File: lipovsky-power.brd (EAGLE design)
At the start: 59 x 32 mm, 95 parts, among them J1 M04-929J, J2 M04-929J, J3 M04-929J, J4 M04-929J, Q1 NMOS30V_30A, Q12 NMOS40V_10A, Q14 NMOS40V_10A, Q16 NMOS40V_10A, Q18 NMOS40V_10A, Q21 PMOS30V_11A, Q22 PMOS30V_11A, Q23 NMOS40V_10A, Q24 NMOS40V_10A, Q25 PMOS30V_11A, Q26 PMOS30V_11A, Q27 NMOS40V_10A, Q28 NMOS40V_10A, Q3 2PMOS50V_0.17A, Q31 PMOS30V_11A, Q32 PMOS30V_11A, Q33 PMOS30V_11A, Q34 PMOS30V_11A, Q35 PMOS30V_11A, Q36 PMOS30V_11A, Q37 PMOS30V_11A, Q38 PMOS30V_11A, Q4 2PMOS50V_0.17A, Q41 PMOS30V_11A, Q42 PMOS30V_11A, Q43 PMOS30V_11A, Q44 PMOS30V_11A, Q45 PMOS30V_11A, Q46 PMOS30V_11A, Q47 PMOS30V_11A, Q48 PMOS30V_11A, Q5 2NMOS30V_0.1A, Q51 PMOS30V_11A, Q52 PMOS30V_11A, Q53 PMOS30V_11A, Q54 PMOS30V_11A, Q55 PMOS30V_11A, Q56 PMOS30V_11A, Q57 PMOS30V_11A, Q58 PMOS30V_11A, Q62 PMOS30V_11A, Q64 PMOS30V_11A, Q66 PMOS30V_11A, Q68 PMOS30V_11A, T1 TFORM_4_4311_4A4, U1 DG508BEN-T1-GE4, U2 DG508BEN-T1-GE4, U4 LTC3805-5IDD, U6 AR30N60PPA-13

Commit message: tidy
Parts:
- MVOE: value ATTINYX4A4MMH -> ATTINYX4A2MMHR
- moved R16 2.39 mm to (43.0, 26.1), turned to 90 degrees
- moved C8 1.64 mm to (41.9, 26.8)
- moved RGS 0.22 mm to (19.2, 25.1)
- moved R10 0.20 mm to (43.4, 28.0)
- moved RGS6 0.10 mm to (26.5, 25.8)
- turned R3 to 0 degrees
- turned R4 to 0 degrees
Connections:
- removed net !RESET: J3.4, MVOE.13, R3.2
- new net !S_RESET: J3.4, MVOE.13, R3.1
- net +5V: now also R3.2, R4.2; no longer R3.1, R4.1
- net SDA: now also R4.1; no longer R4.2
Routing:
- net !RESET: track 9.34 -> 0.00 mm, vias 1 -> 0
- net !S_RESET: track 0.00 -> 9.34 mm, vias 0 -> 1
- net S-: track 142.4 -> 138.3 mm, vias 19 -> 18
- net EN_FLYBACK: track 11.8 -> 10.1 mm, vias 3 -> 2
- net +5V: track 41.9 -> 41.3 mm
- net AS2: track 23.2 -> 22.7 mm, vias 3 -> 2
- net AS1: track 23.7 -> 23.4 mm, vias 3 -> 2
- net AS0: track 24.2 -> 24.1 mm, vias 3 -> 2
- net BATT-: vias 40 -> 41

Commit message: Moved fet
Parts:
- moved Q3 19.4 mm to (15.4, 7.60), turned to 180 degrees
- moved C7 4.00 mm to (16.4, 26.7)
- moved RGS-2 3.86 mm to (13.0, 6.40)
- moved RGS1 2.50 mm to (16.8, 6.40)
- moved C1 2.02 mm to (14.0, 6.40)
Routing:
- net !GS1: track 7.31 -> 34.9 mm
- net GS1: track 28.9 -> 11.7 mm, vias 4 -> 2
- net GS-2: track 33.1 -> 16.5 mm, vias 4 -> 3
- net GS+2: track 30.9 -> 37.7 mm, vias 4 -> 5
- net C4+: track 52.4 -> 46.9 mm, vias 4 -> 3
- net BATT+: track 69.9 -> 69.2 mm
- net BATT-: vias 41 -> 42

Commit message: tidy
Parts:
- moved TP1 1.00 mm to (41.0, 30.0)
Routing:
- net S-: track 138.3 -> 142.7 mm, vias 18 -> 19
- net MISO: track 4.87 -> 5.87 mm
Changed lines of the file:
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@@
 <vertex x="28" y="11.175"/>
 </polygon>
-<text x="41.1" y="30" size="0.8" layer="22" font="vector" ratio="15" distance="75" rot="MR90" align="top-center">MISO</text>
+<text x="40.1" y="30.1" size="0.8" layer="22" font="vector" ratio="15" distance="75" rot="MR90" align="top-center">MISO</text>
 </plain>
 <attributes>
@@
 <attribute name="TEMP" value="±100ppm/°C" x="43" y="26.1" size="1.778" layer="27" rot="R90" display="off"/>
 </element>
-<element name="TP1" library="SparkFun-Passives" package="PAD.03X.03" value="TEST-POINT3" x="42" y="30" rot="MR0"/>
+<element name="TP1" library="SparkFun-Passives" package="PAD.03X.03" value="TEST-POINT3" x="41" y="30" rot="MR0"/>
 </elements>
 <signals>
@@
 <wire x1="32.6" y1="24.2" x2="32.6" y2="22.6" width="0.8" layer="1"/>
 <wire x1="32.6" y1="22.6" x2="32.3" y2="22.3" width="0.8" layer="1"/>
-<wire x1="27" y1="27.6" x2="30.9" y2="23.7" width="0.3" layer="15"/>
+<wire x1="27" y1="27.6" x2="30.5" y2="24.1" width="0.3" layer="15"/>
 <wire x1="25.2" y1="5.275" x2="25.2" y2="4.9" width="0.2" layer="1"/>
 <wire x1="25.2" y1="4.9" x2="25.4" y2="4.7" width="0.2" layer="1"/>
@@
 <wire x1="20.575" y1="22.95" x2="19.925" y2="22.95" width="0.7" layer="2"/>
 <wire x1="44.19" y1="6.31" x2="44.19" y2="2" width="0.3" layer="16"/>
-<wire x1="30.9" y1="23.7" x2="31.1" y2="23.3" width="0.3" layer="15"/>
 <wire x1="18" y1="23.1" x2="18.15" y2="22.95" width="0.3" layer="1"/>
 <wire x1="18.15" y1="22.95" x2="19.275" y2="22.95" width="0.3" layer="1"/>
@@
 <wire x1="49.71" y1="27.9" x2="48" y2="27.9" width="0.3" layer="16"/>
 <wire x1="48" y1="27.9" x2="47" y2="26.9" width="0.3" layer="16"/>
-<wire x1="46.5" y1="25.1" x2="46.5" y2="25.8" width="0.2" layer="1"/>
+<wire x1="46.5" y1="25.05" x2="46.5" y2="25.8" width="0.2" layer="1"/>
 <wire x1="41.7" y1="24.8" x2="42.1" y2="24.4" width="0.3" layer="16"/>
 <wire x1="42.1" y1="24.4" x2="42.1" y2="24" width="0.3" layer="16"/>
@@
 <wire x1="43" y1="25.6" x2="42.2" y2="25.6" width="0.4" layer="1"/>
 <wire x1="42.2" y1="25.6" x2="42.1" y2="25.5" width="0.4" layer="1"/>
-<wire x1="46.5" y1="25.1" x2="46.5" y2="25.05" width="0" layer="19" extent="1-1"/>
+<via x="30.5" y="23.65" extent="1-16" drill="0.4"/>
+<wire x1="31.1" y1="23.3" x2="30.5" y2="23.65" width="0.7" layer="15"/>
+<wire x1="30.5" y1="23.65" x2="30.5" y2="22.95" width="0.7" layer="15"/>
+<wire x1="30.5" y1="22.95" x2="30.5" y2="23.65" width="0.7" layer="1"/>
+<wire x1="30.5" y1="23.65" x2="31.1" y2="23.3" width="0.7" layer="1"/>
+<wire x1="30.5" y1="23.65" x2="30.5" y2="22.95" width="0.7" layer="2"/>
+<wire x1="31.1" y1="23.3" x2="30.5" y2="23.65" width="0.7" layer="2"/>
+<wire x1="31.1" y1="23.3" x2="30.5" y2="23.65" width="0.7" layer="16"/>
+<wire x1="30.5" y1="24.1" x2="30.5" y2="23.65" width="0.3" layer="15"/>
 </signal>
 <signal name="S+">
@@
 <wire x1="45.6" y1="27.85" x2="45.6" y2="28.5" width="0.2" layer="1"/>
 <contactref element="TP1" pad="P$1"/>
-<wire x1="45.6" y1="28.5" x2="43.5" y2="28.5" width="0.3" layer="16"/>
-<wire x1="43.5" y1="28.5" x2="42" y2="30" width="0.3" layer="16"/>
+<wire x1="45.6" y1="28.5" x2="42.5" y2="28.5" width="0.3" layer="16"/>
+<wire x1="42.5" y1="28.5" x2="41" y2="30" width="0.3" layer="16"/>
 </signal>
 </signals>

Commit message: neverending gilding
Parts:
- removed R10, R4: RES5.1K_16, dubec:0402
- added TP2: TEST-POINT3, SparkFun-Passives:PAD.03X.03
- moved C1 1.08 mm to (13.0, 6.80)
- moved RGS-2 1.08 mm to (14.0, 6.80)
- moved R3 0.72 mm to (49.6, 25.9), turned to 270 degrees
- moved R16 0.30 mm to (43.0, 26.4)
- moved R8 0.20 mm to (30.3, 25.9)
- moved R9 0.20 mm to (30.3, 24.9)
- moved C2 0.20 mm to (32.1, 25.4)
- moved RGT 0.10 mm to (21.3, 6.00)
- moved RGT+2 0.10 mm to (21.3, 8.40)
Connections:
- net +5V: no longer R10.1, R4.2
- net N$8: now also TP2.P$1
- net SCL: no longer R10.2
- net SDA: no longer R4.1
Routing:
- net S-: track 142.7 -> 35.3 mm, vias 19 -> 20
- net BATT-: track 4.18 -> 32.2 mm, vias 42 -> 41
- net GS-2: track 16.5 -> 8.66 mm, vias 3 -> 2
- net T+: track 54.7 -> 47.0 mm
- net GT6: track 37.6 -> 32.6 mm
- net N$8: track 5.66 -> 2.00 mm, vias 1 -> 0
- net +5V: track 41.3 -> 37.8 mm
- net GS+2: track 37.7 -> 39.6 mm, vias 5 -> 4
- net SDA: track 4.62 -> 2.92 mm
- net N$5: track 20.9 -> 22.4 mm
- net BATT+: track 69.2 -> 67.7 mm
- net GS1: track 11.7 -> 13.2 mm
- net SFB: track 7.71 -> 9.11 mm
- net S+: track 29.9 -> 28.6 mm
- net !GS1: track 34.9 -> 33.8 mm
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- added copper zone on layer 15, net S-
- added copper zone on layer 2, net S-
- removed copper zone on layer 15, net BATT-
- removed copper zone on layer 2, net BATT-

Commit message: tweaks
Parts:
- turned U$1 to 0 degrees
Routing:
- net BATT-: track 32.2 -> 22.0 mm, vias 41 -> 37
- net S-: track 35.3 -> 35.9 mm, vias 20 -> 19
- added copper zone on layer 2, net BATT-

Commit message: diode conf
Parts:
- removed D2: 4DSCH30V_0A1, dubec:8-HMD
- added R4: RES15.4K_16, dubec:0402
- added U$3, U$4: 3DSCH40V_0.35A, dubec:SOT-363
- D1: value 4DSCH30V_0A1 -> D_ZENER18V_0.3W; device dubec:8-HMD -> dubec:SOD323+
- moved D1 4.52 mm to (14.4, 4.95), turned to 180 degrees
- moved C1 1.04 mm to (12.0, 6.50), turned to 90 degrees
- moved RGS-2 0.30 mm to (14.0, 6.50)
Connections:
- net BATT+: now also R4.2, U$3.1, U$3.2, U$3.3, U$4.1, U$4.2, U$4.3, U$4.4; no longer D2.5, D2.6, D2.7
- net BATT-: now also D1.A; no longer D2.1, D2.8
- net C2: now also U$3.6; no longer D1.1
- net C3: now also U$3.5; no longer D1.2
- net C4: now also U$3.4; no longer D1.3
- net C4+: now also D1.C, R4.1; no longer D1.4, D1.5, D1.6, D1.7, D1.8, D2.2
- net C5: now also U$4.5; no longer D2.3
- net C6: now also U$4.6; no longer D2.4
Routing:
- net BATT+: track 67.6 -> 93.1 mm, vias 6 -> 8
- net C4+: track 47.5 -> 26.3 mm, vias 4 -> 3
- net C4: track 23.4 -> 21.6 mm
- net C5: track 20.0 -> 21.6 mm
- net C6: track 4.38 -> 5.65 mm
- net C3: track 20.6 -> 19.8 mm

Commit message: tweaks
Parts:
- moved RGS6 0.92 mm to (26.7, 26.7), turned to 270 degrees
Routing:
- net BATT+: track 93.1 -> 72.9 mm, vias 8 -> 7
- net !GT1: track 8.35 -> 12.5 mm
- net T-: track 43.5 -> 45.7 mm
- net AT0: track 41.0 -> 43.0 mm
- net C4+: track 26.3 -> 24.8 mm
- net GT+2: track 21.2 -> 22.5 mm
- net GT5: track 32.8 -> 31.8 mm
- net GT4: track 31.4 -> 30.4 mm
- net GT6: track 32.6 -> 32.0 mm
- net S-: vias 19 -> 18

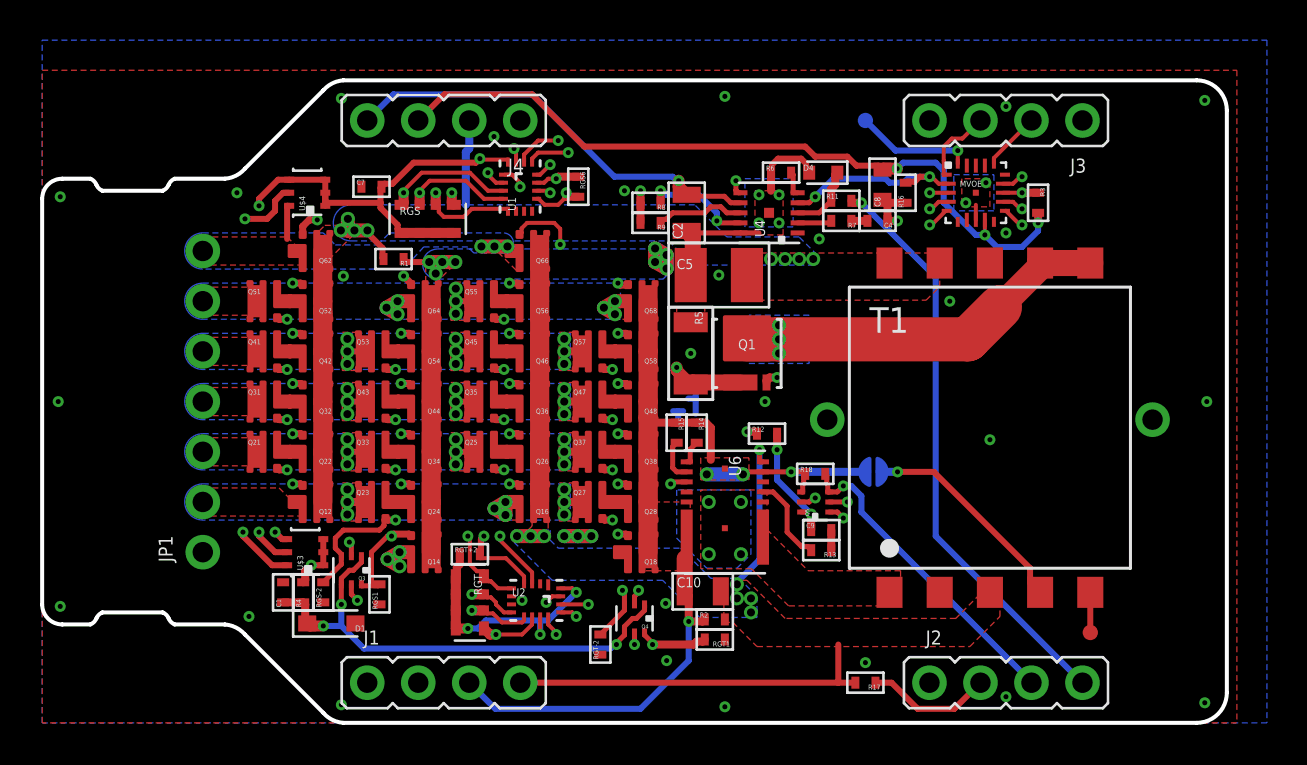
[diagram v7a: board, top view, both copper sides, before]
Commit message: Connector pin reordering
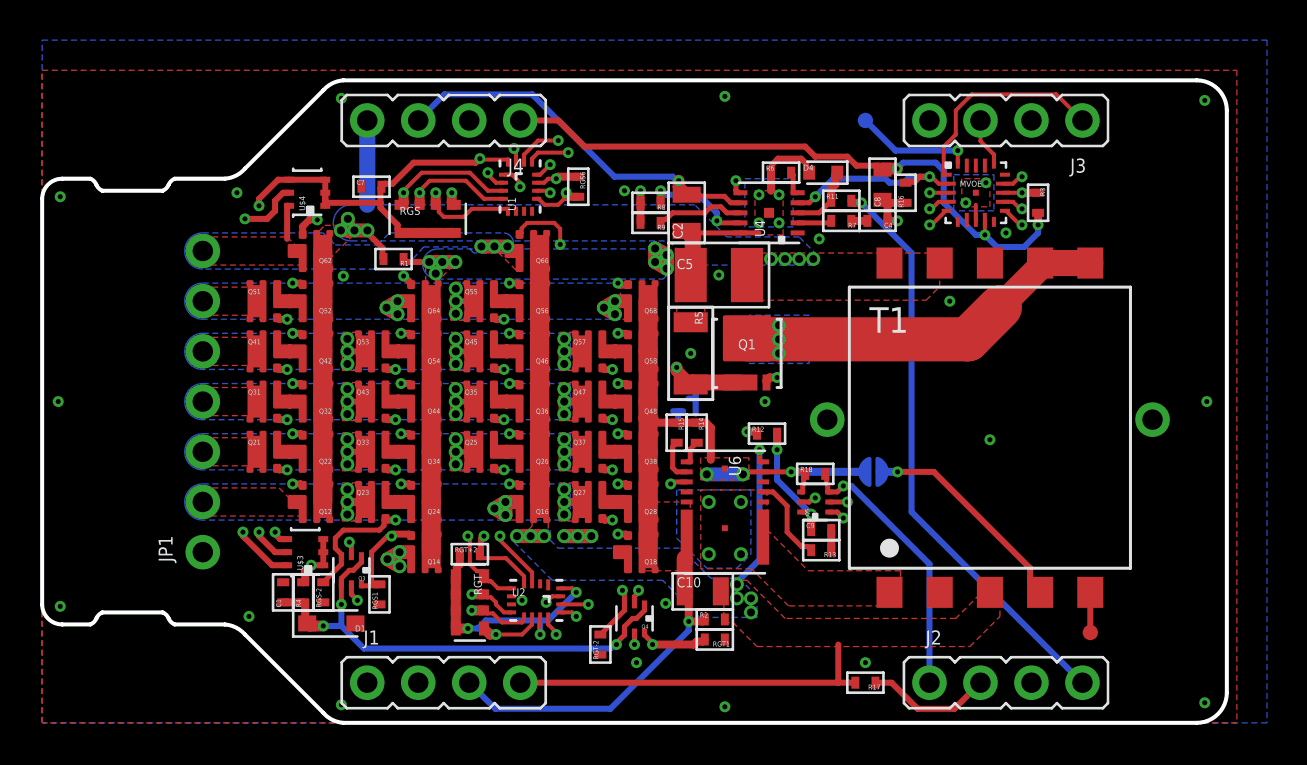
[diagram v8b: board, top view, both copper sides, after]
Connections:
- net +5V: now also J4.1; no longer J4.3
- net +8V: now also J4.3; no longer J4.4
- net OPTO_C: now also J2.1; no longer J2.3
- net S+: now also J4.4; no longer J4.2
- net S-: now also J2.3, J3.2, J4.2; no longer J2.1, J3.1, J4.1
- net SCL: now also J3.1; no longer J3.3
- net SDA: now also J3.3; no longer J3.2
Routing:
- net SCL: track 3.92 -> 10.8 mm
- net +5V: track 37.8 -> 31.7 mm
- net +8V: track 36.7 -> 34.2 mm
- net OPTO_C: track 15.8 -> 13.7 mm
- net BATT-: track 22.1 -> 23.4 mm, vias 37 -> 34
- net T-: track 45.7 -> 44.9 mm
